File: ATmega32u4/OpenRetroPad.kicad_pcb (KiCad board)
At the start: 4 copper layers, 46 x 74 mm, 69 parts, among them J1 USB_C_Receptacle_USB2.0, J2 USB_C_Receptacle_USB2.0, J3 NRF24, J4 DB25_Male_MountingHoles, SW1 HWB, SW2 RESET, U1 AMS1117-3.3, U2 ATmega32U4-M, U3 CH330N, U4 USBLC6-2SC6, U5 USBLC6-2SC6, Y1 16MHz

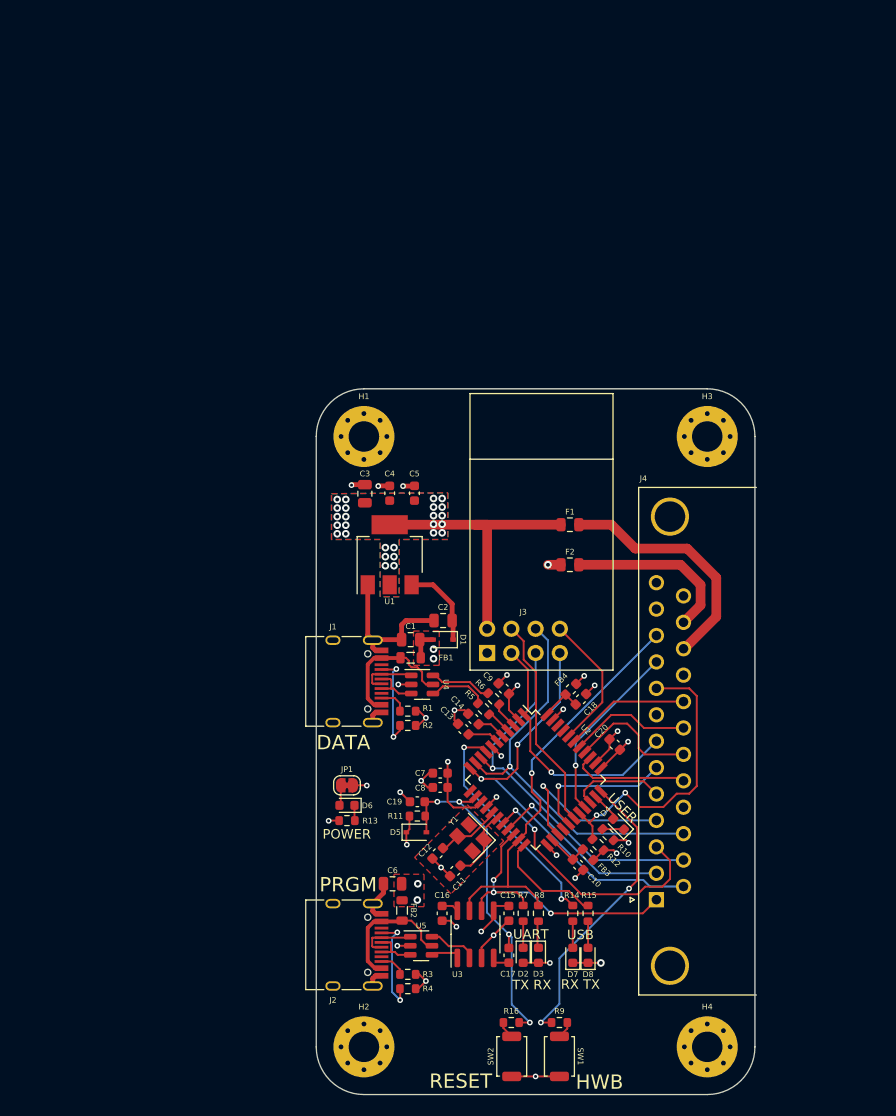
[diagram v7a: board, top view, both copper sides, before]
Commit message: Review and updates to power path
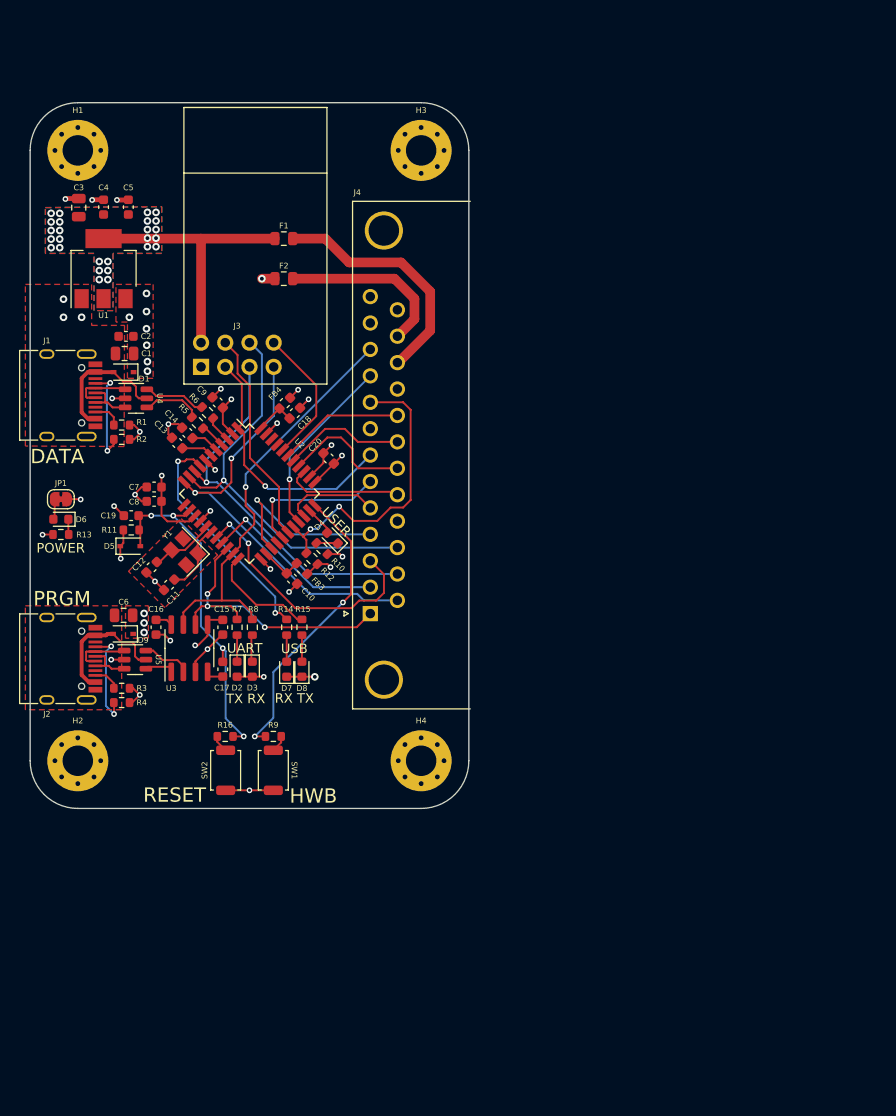
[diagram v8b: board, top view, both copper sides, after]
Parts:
- removed FB1, FB2: 500mA, Inductor_SMD:L_0805_2012Metric
- added D9: D_Schottky, Diode_SMD:D_SOD-323, F.Cu at (74.8, 120.7)
- C2: value 10u -> 1u; footprint Capacitor_SMD:C_0805_2012Metric -> Capacitor_SMD:C_0603_1608Metric
- D1: value 1N5817 -> D_Schottky
- moved C2 44.6 mm to (75.0, 89.5)
- moved D1 43.7 mm to (74.8, 93.2)
- moved C11 42.4 mm to (79.6, 115.5)
- moved C13 42.4 mm to (80.4, 100.7)
- moved C19 42.4 mm to (75.6, 108.3)
- moved C20 42.4 mm to (96.3, 102.3)
- moved C7 42.4 mm to (78.0, 105.3)
- moved C8 42.4 mm to (78.0, 106.8)
- moved J2 42.4 mm to (67.8, 123.3)
- moved R1 42.4 mm to (74.6, 98.8)
- moved R11 42.4 mm to (75.6, 109.8)
- moved R12 42.4 mm to (94.5, 112.8)
- moved R13 42.4 mm to (68.2, 110.3)
- moved R2 42.4 mm to (74.6, 100.3)
- moved R5 42.4 mm to (82.5, 98.6)
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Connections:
- C2 pad 2: /Power/VREGIN -> +5V
- D1 pad 1: /Power/VREGIN -> +5V
- D1 pad 2: +5V -> /USB Data/VBUS
- U1 pad 3: /Power/VREGIN -> +5V
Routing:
- net GND: track 76.7 -> 52.9 mm, vias 24 -> 27
- net /Power/VREGIN: track 8.87 -> 0.00 mm
- net +5V: track 39.1 -> 35.9 mm, vias 15 -> 21
- net +3V3: track 30.2 -> 28.8 mm
